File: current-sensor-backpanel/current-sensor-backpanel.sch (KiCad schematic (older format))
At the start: 3 parts, among them J1 Conn_01x01_Female, J2 Conn_01x01_Female

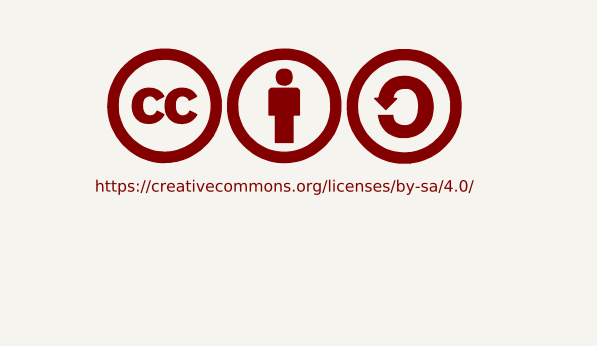
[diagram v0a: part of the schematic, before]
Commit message: complete mechanical placement of all components on main pcb, and holes on front/back panels
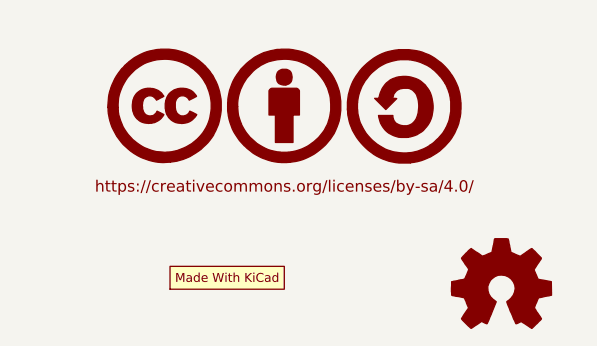
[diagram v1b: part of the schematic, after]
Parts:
- added LOGO2: Logo_MadeWithKiCad, Symbol:KiCad-Logo2_6mm_SilkScreen, symbol Graphic_gkeeth:Logo_MadeWithKiCad
- added LOGO3: Logo_Open_Hardware_Small, Symbol:OSHW-Logo2_7.3x6mm_SilkScreen, symbol Graphic:Logo_Open_Hardware_Small
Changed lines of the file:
@@
+	1    0    0    -1
+$EndComp
+$Comp
+L Graphic:Logo_Open_Hardware_Small LOGO3
+U 1 1 5F35F18D
+P 5200 7650
+F 0 "LOGO3" H 5200 7925 50  0001 C CNN
+F 1 "Logo_Open_Hardware_Small" H 5200 7425 50  0001 C CNN
+F 2 "Symbol:OSHW-Logo2_7.3x6mm_SilkScreen" H 5200 7650 50  0001 C CNN
+F 3 "~" H 5200 7650 50  0001 C CNN
+	1    5200 7650
+	1    0    0    -1
+$EndComp
+$Comp
+L Graphic_gkeeth:Logo_MadeWithKiCad LOGO2
+U 1 1 5F35F508
+P 4000 7650
+F 0 "LOGO2" H 4000 7650 50  0001 C CNN
+F 1 "Logo_MadeWithKiCad" H 4000 7650 50  0001 C CNN
+F 2 "Symbol:KiCad-Logo2_6mm_SilkScreen" H 4000 7650 50  0001 C CNN
+F 3 "" H 4000 7650 50  0001 C CNN
+	1    4000 7650
 	1    0    0    -1
 $EndComp

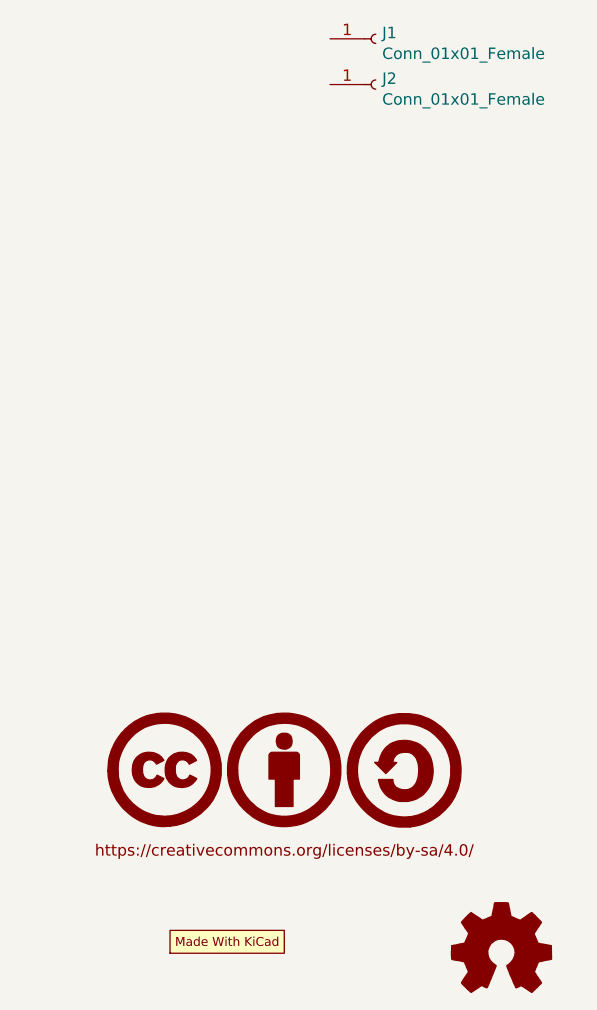
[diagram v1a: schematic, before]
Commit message: add back panel label
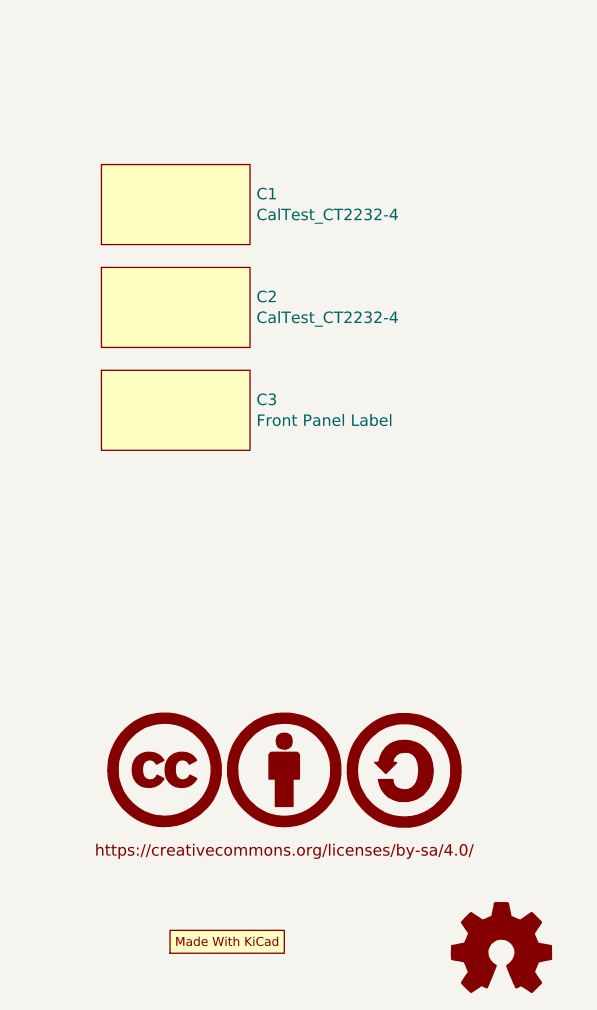
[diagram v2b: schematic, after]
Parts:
- removed J1, J2: Conn_01x01_Female, Panel_Cutouts:BindingPost_Pomona_3750_3760_3770, symbol Connector:Conn_01x01_Female
- added C1, C2: CalTest_CT2232-4, Panel_Cutouts:Panel_BindingPost_CalTest_CT2232-x, symbol Panel_Cutouts:Panel_Cutout
- added C3: Front Panel Label, current-sensor:backpanel, symbol Panel_Cutouts:Panel_Cutout
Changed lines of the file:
@@
 encoding utf-8
 Sheet 1 1
-Title ""
-Date ""
-Rev ""
-Comp ""
+Title "current-sensor Back Panel"
+Date "2020-10-25"
+Rev "0"
+Comp "G. Keeth"
 Comment1 ""
 Comment2 ""
@@
 F 3 "" H 4250 6850 50  0001 C CNN
 	1    4250 6850
-	1    0    0    -1
-$EndComp
-$Comp
-L Connector:Conn_01x01_Female J1
-U 1 1 5F307A67
-P 4650 3650
-F 0 "J1" H 4678 3676 50  0000 L CNN
-F 1 "Conn_01x01_Female" H 4678 3585 50  0000 L CNN
-F 2 "Panel_Cutouts:BindingPost_Pomona_3750_3760_3770" H 4650 3650 50  0001 C CNN
-F 3 "~" H 4650 3650 50  0001 C CNN
-F 4 "Pomona" H 4650 3650 50  0001 C CNN "Manufacturer"
-F 5 "3760-4" H 4650 3650 50  0001 C CNN "Manufacturer PN"
-	1    4650 3650
-	1    0    0    -1
-$EndComp
-$Comp
-L Connector:Conn_01x01_Female J2
-U 1 1 5F308475
-P 4650 3850
-F 0 "J2" H 4678 3876 50  0000 L CNN
-F 1 "Conn_01x01_Female" H 4678 3785 50  0000 L CNN
-F 2 "Panel_Cutouts:BindingPost_Pomona_3750_3760_3770" H 4650 3850 50  0001 C CNN
-F 3 "~" H 4650 3850 50  0001 C CNN
-F 4 "Pomona" H 4650 3850 50  0001 C CNN "Manufacturer"
-F 5 "3760-4" H 4650 3850 50  0001 C CNN "Manufacturer PN"
-	1    4650 3850
 	1    0    0    -1
 $EndComp
@@
 	1    0    0    -1
 $EndComp
+$Comp
+L Panel_Cutouts:Panel_Cutout C1
+U 1 1 5F95E7A6
+P 3450 4150
+F 0 "C1" H 4128 3971 50  0000 L CNN
+F 1 "CalTest_CT2232-4" H 4128 3880 50  0000 L CNN
+F 2 "Panel_Cutouts:Panel_BindingPost_CalTest_CT2232-x" H 3450 4150 50  0001 C CNN
+F 3 "" H 3450 4150 50  0001 C CNN
+	1    3450 4150
+	1    0    0    -1
+$EndComp
+$Comp
+L Panel_Cutouts:Panel_Cutout C2
+U 1 1 5F95EB1D
+P 3450 4600
+F 0 "C2" H 4128 4421 50  0000 L CNN
+F 1 "CalTest_CT2232-4" H 4128 4330 50  0000 L CNN
+F 2 "Panel_Cutouts:Panel_BindingPost_CalTest_CT2232-x" H 3450 4600 50  0001 C CNN
+F 3 "" H 3450 4600 50  0001 C CNN
+	1    3450 4600
+	1    0    0    -1
+$EndComp
+$Comp
+L Panel_Cutouts:Panel_Cutout C3
+U 1 1 5F96214B
+P 3450 5050
+F 0 "C3" H 4128 4871 50  0000 L CNN
+F 1 "Front Panel Label" H 4128 4780 50  0000 L CNN
+F 2 "current-sensor:backpanel" H 3450 5050 50  0001 C CNN
+F 3 "" H 3450 5050 50  0001 C CNN
+	1    3450 5050
+	1    0    0    -1
+$EndComp
